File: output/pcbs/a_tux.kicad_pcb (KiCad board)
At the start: 2 copper layers, 136.8 x 108.6 mm, 39 parts

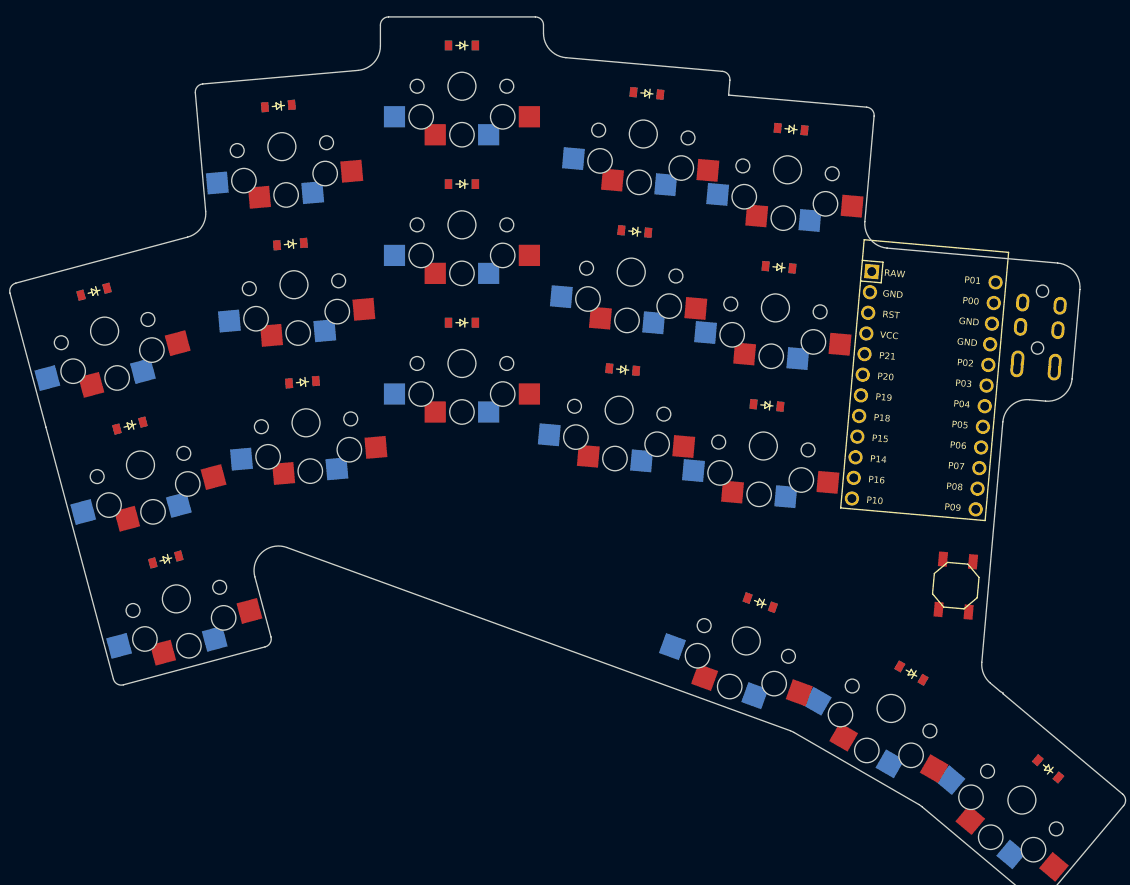
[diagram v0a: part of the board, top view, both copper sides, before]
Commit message: Added hotswap + solder option for switches, moved diode locations, moved stuff around to make routing easier
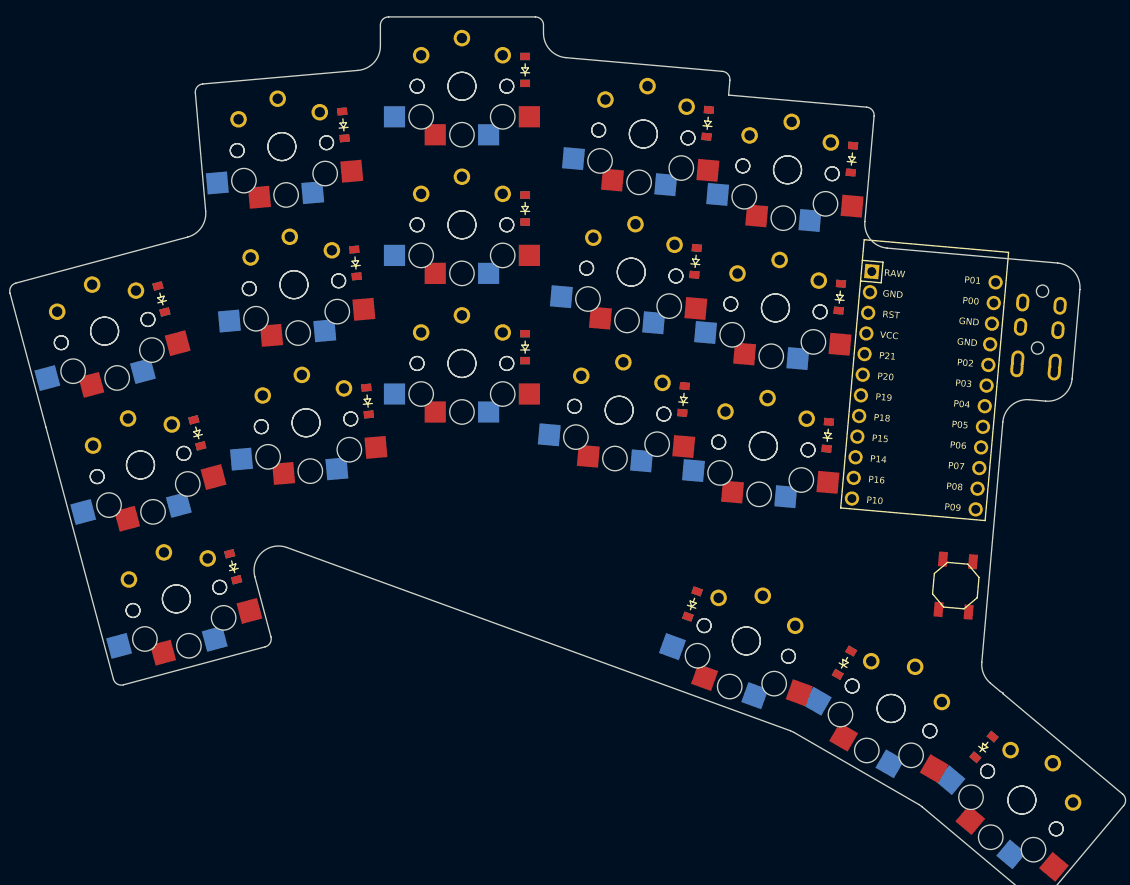
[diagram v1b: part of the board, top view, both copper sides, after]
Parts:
- added S19, S20: , PG1350, F.Cu at (67.9, -22.6)
- added S21, S22: , PG1350, F.Cu at (69.4, -39.5)
- added S23, S24: , PG1350, F.Cu at (70.9, -56.4)
- added S25, S26: , PG1350, F.Cu at (85.6, -18.2)
- added S27, S28: , PG1350, F.Cu at (87.1, -35.1)
- added S29, S30: , PG1350, F.Cu at (88.6, -52.0)
- added S31, S32: , PG1350, F.Cu at (83.5, 5.74)
- added S33, S34: , PG1350, F.Cu at (101.3, 14.0)
- added S35, S36: , PG1350, F.Cu at (117.3, 25.3)
- moved S18 111.3 mm to (48.6, -62.3), turned to 0 degrees
- moved S17 92.7 mm to (48.6, -62.3), turned to 180 degrees
- moved S16 61.8 mm to (48.6, -45.3), turned to 0 degrees
- moved S11 45.5 mm to (26.5, -54.9), turned to 185 degrees
- moved S12 44.4 mm to (26.5, -54.9), turned to 5 degrees
- moved S10 42.7 mm to (28.0, -38.0), turned to 5 degrees
- moved S15 40.5 mm to (48.6, -45.3), turned to 180 degrees
- moved S14 39.0 mm to (48.6, -28.3), turned to 0 degrees
- moved S13 38.3 mm to (48.6, -28.3), turned to 180 degrees
- moved S9 31.9 mm to (28.0, -38.0), turned to 185 degrees
- moved S6 31.4 mm to (4.80, -32.3), turned to 15 degrees
- moved S8 30.9 mm to (29.5, -21.0), turned to 5 degrees
- moved S5 23.9 mm to (4.80, -32.3), turned to 195 degrees
- moved S4 21.0 mm to (9.20, -15.8), turned to 15 degrees
- moved S7 20.5 mm to (29.5, -21.0), turned to 185 degrees
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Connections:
- S10 pad 1: index_bottom -> ring_home
- S10 pad 2: P6 -> P8
- S11 pad 1: index_home -> ring_top
- S11 pad 2: P6 -> P8
- S12 pad 1: index_top -> ring_top
- S12 pad 2: P6 -> P8
- S13 pad 1: inner_bottom -> middle_bottom
- S13 pad 2: P5 -> P7
- S14 pad 1: inner_home -> middle_bottom
- S14 pad 2: P5 -> P7
- S15 pad 1: inner_top -> middle_home
- S15 pad 2: P5 -> P7
- S16 pad 1: first_only -> middle_home
- S17 pad 1: second_only -> middle_top
- S17 pad 2: P6 -> P7
- S18 pad 1: third_only -> middle_top
- S18 pad 2: P5 -> P7
- S2 pad 1: pinky_home -> pinky_bottom
- S3 pad 1: pinky_top -> pinky_home
- S4 pad 1: ring_bottom -> pinky_home
- S4 pad 2: P8 -> P9
- S5 pad 1: ring_home -> pinky_top
- S5 pad 2: P8 -> P9
- S6 pad 1: ring_top -> pinky_top
- S6 pad 2: P8 -> P9
- S7 pad 1: middle_bottom -> ring_bottom
- S7 pad 2: P7 -> P8
- S8 pad 1: middle_home -> ring_bottom
- S8 pad 2: P7 -> P8
- S9 pad 1: middle_top -> ring_home
- S9 pad 2: P7 -> P8

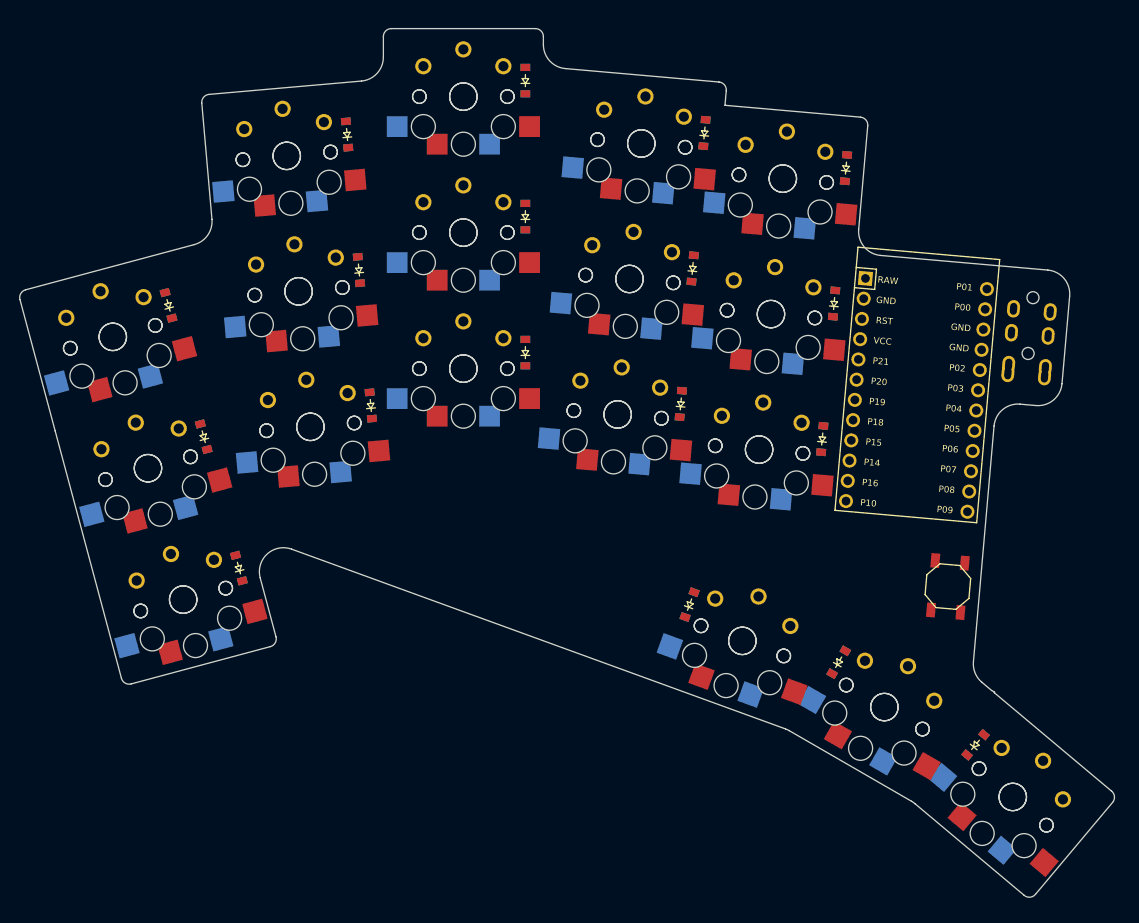
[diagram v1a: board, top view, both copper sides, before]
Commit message: Rotated the outer thumb for 1.5u or 2u keycap.
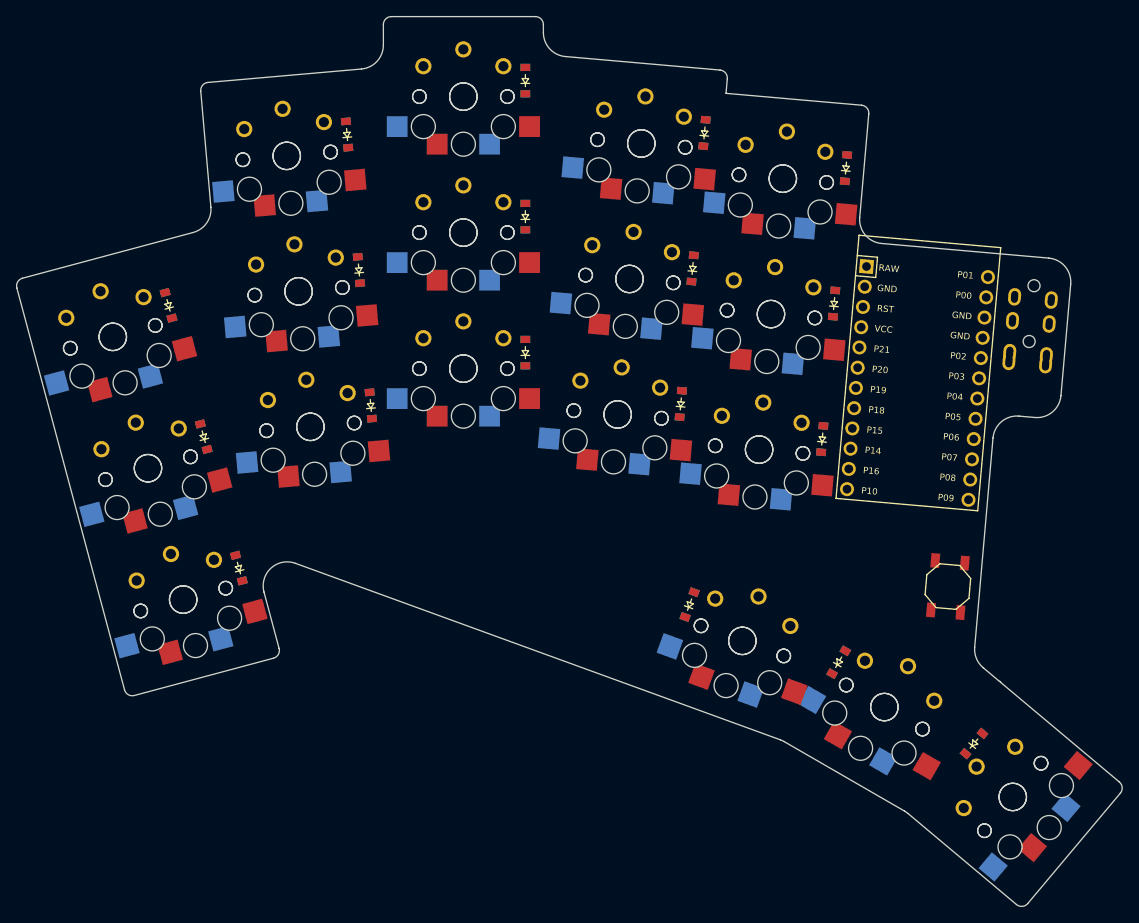
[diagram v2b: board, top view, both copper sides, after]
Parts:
- moved MCU1 1.50 mm to (105.4, -26.5)
- moved REF** 1.50 mm to (122.4, -40.0)
- moved D18 0.25 mm to (112.5, 18.6)
- turned S35 to 230 degrees
- turned S36 to 50 degrees
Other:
- board size 136.8 x 108.6 mm -> 138.2 x 111.2 mm

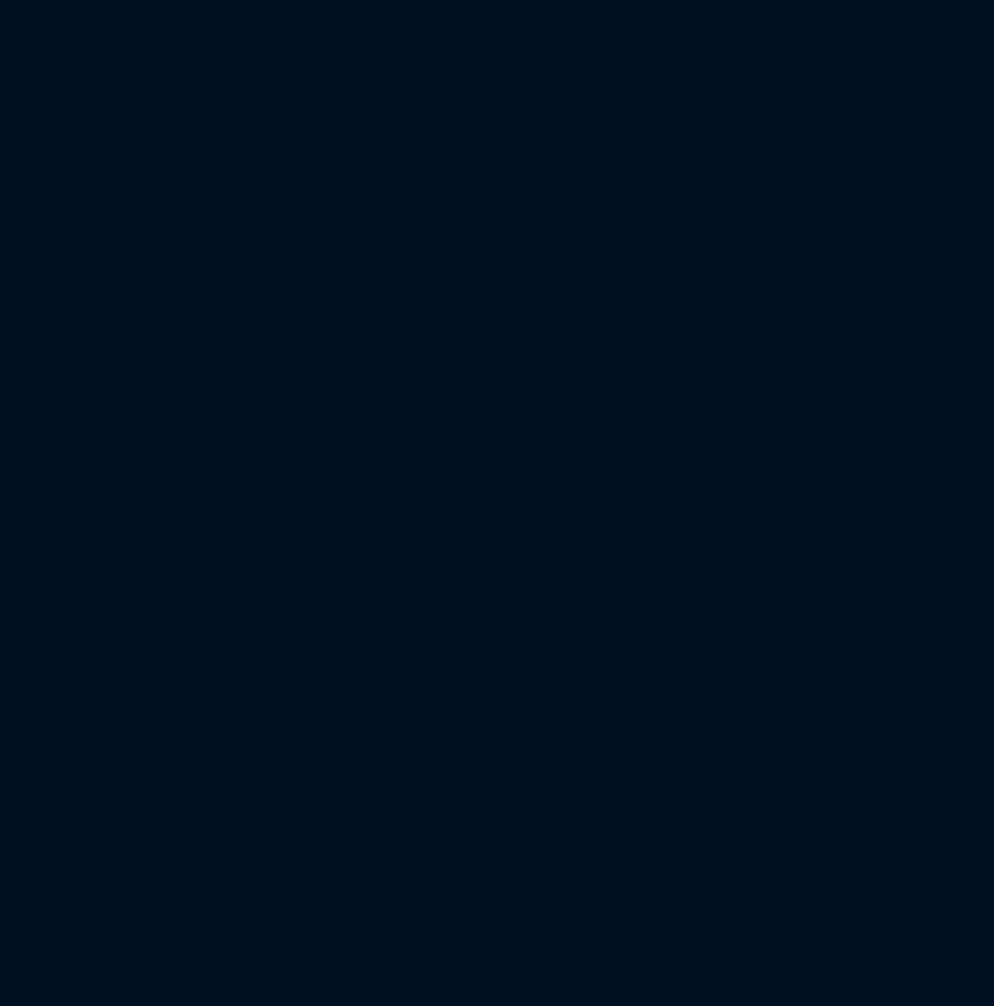
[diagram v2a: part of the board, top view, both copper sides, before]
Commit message: Added Split KB's Puck footprint
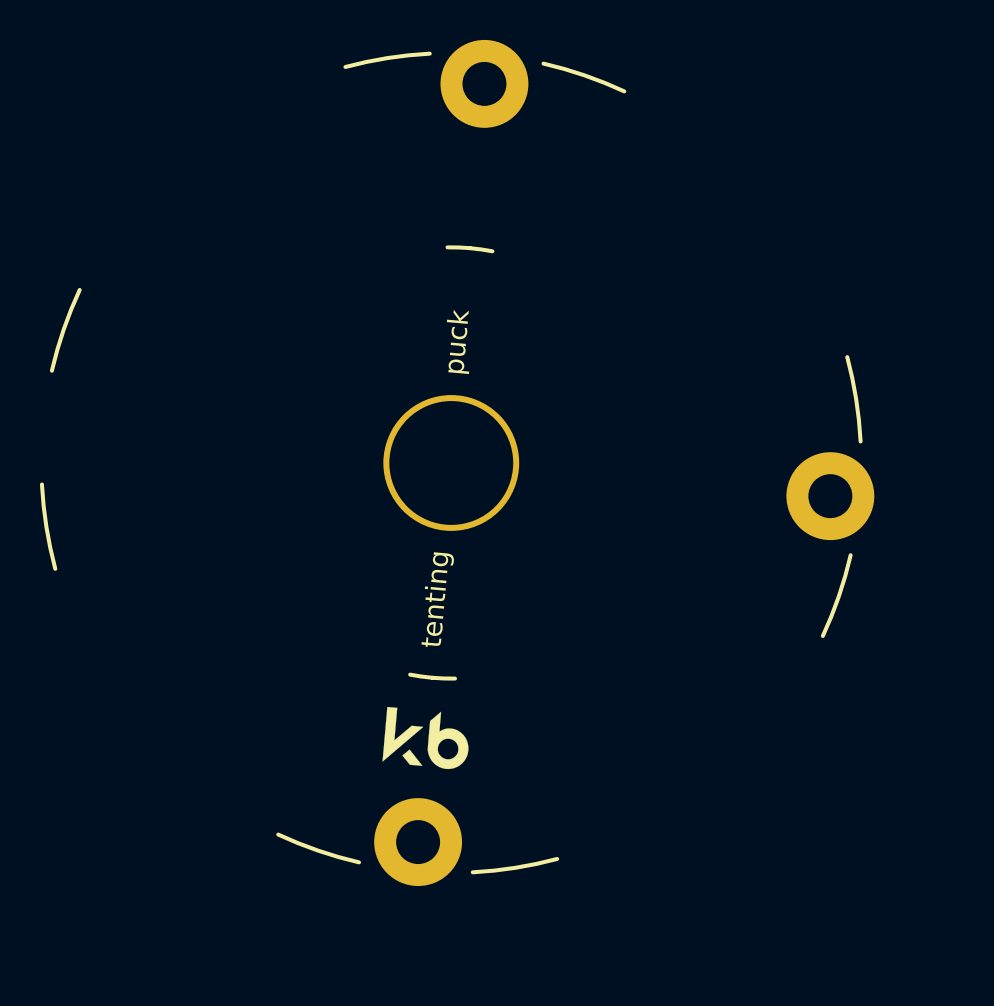
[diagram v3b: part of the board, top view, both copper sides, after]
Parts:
- added _1: Tenting Puck, Tenting Puck, F.Cu at (-112.2, -52.5)

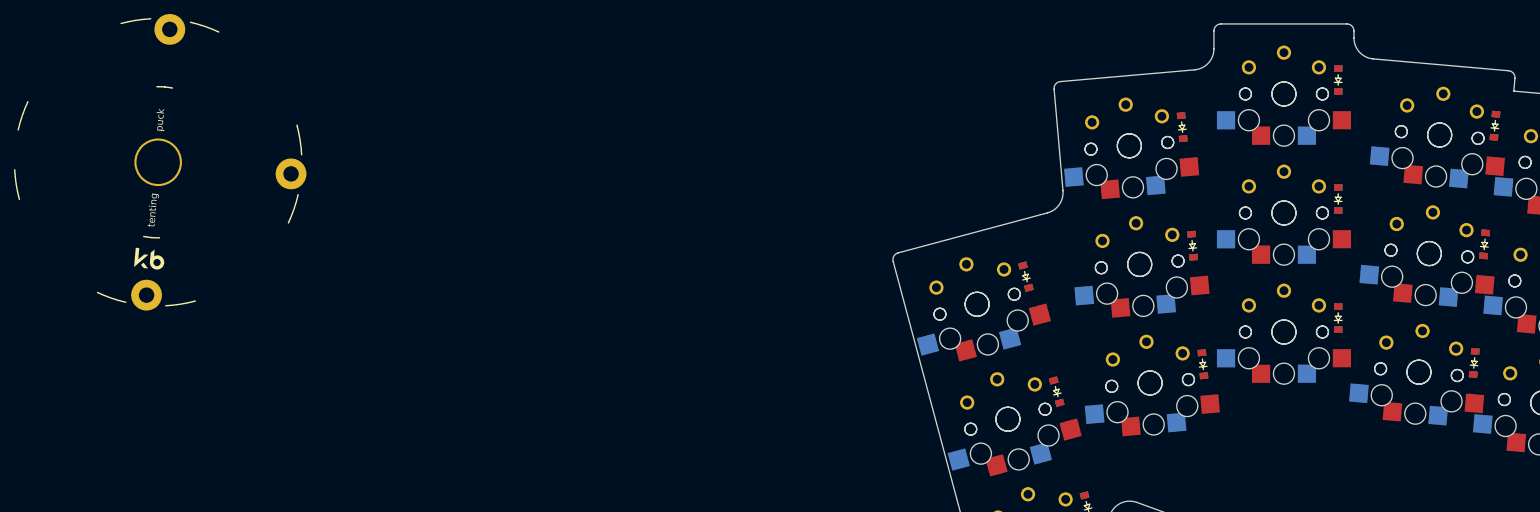
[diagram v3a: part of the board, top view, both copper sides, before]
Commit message: Add puck back to the PCB, fix puck footprint.  Added reversible header footprint
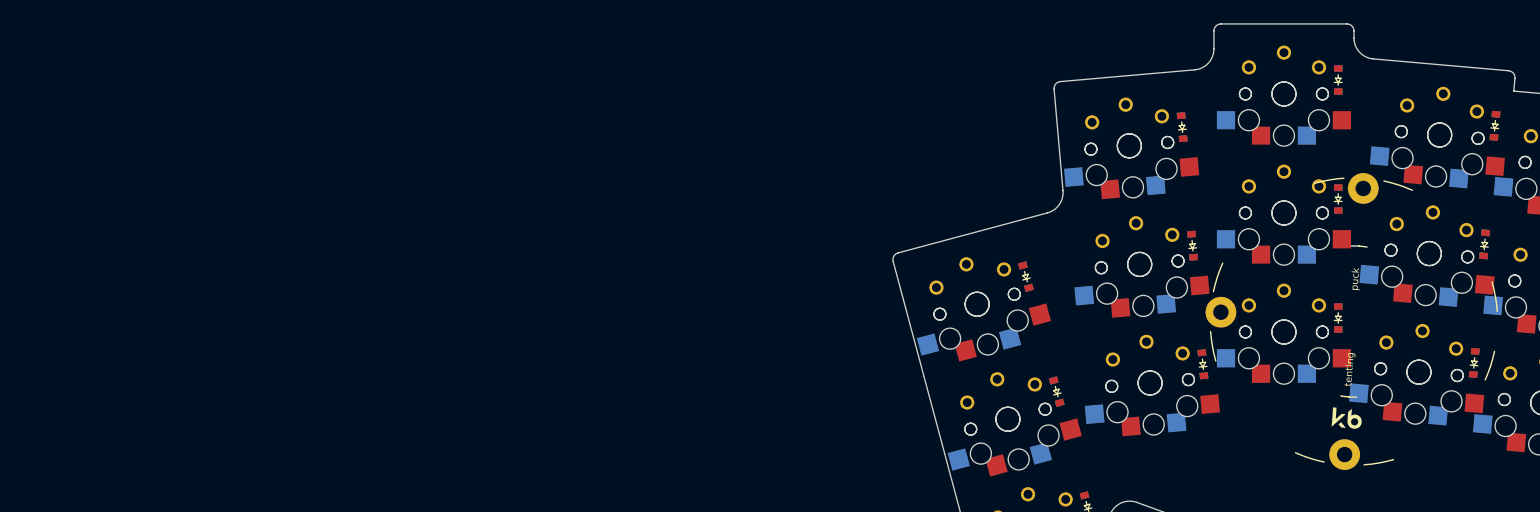
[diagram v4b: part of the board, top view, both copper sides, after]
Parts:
- moved _1 172.3 mm to (58.6, -29.8), turned to -4 degrees
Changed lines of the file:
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@@
       )
 (module "Tenting Puck" (layer F.Cu)
-  (at -112.16671790000001 -52.5371352 -5)
+  (at 58.624363 -29.7933885 -4)
   (fp_text reference "_1" (at 7.6835 1.4605) (layer F.Fab)
     hide
@@
   (fp_arc (start 0 0) (end -20.32 2.8575) (angle -11.96501054) (layer B.SilkS) (width 0.2))
   (fp_arc (start 0 0) (end -20.32 -2.8575) (angle 11.96500434) (layer B.SilkS) (width 0.2))
-  (fp_text user tenting (at -0.1905 6.858 85) (layer F.SilkS)
+  (fp_text user tenting (at -0.1905 6.858 86) (layer F.SilkS)
     (effects (font (size 1 1) (thickness 0.1)))
   )
-  (fp_text user puck (at -0.254 -6.0325 85) (layer F.SilkS)
+  (fp_text user puck (at -0.254 -6.0325 86) (layer F.SilkS)
     (effects (font (size 1 1) (thickness 0.1)))
   )
-  (fp_text user tenting (at -0.254 -6.9215 85) (layer B.SilkS)
+  (fp_text user tenting (at -0.254 -6.9215 86) (layer B.SilkS)
     (effects (font (size 1 1) (thickness 0.1)) (justify mirror))
   )
-  (fp_text user puck (at -0.1905 6.0325 85 unlocked) (layer B.SilkS)
+  (fp_text user puck (at -0.1905 6.0325 86 unlocked) (layer B.SilkS)
     (effects (font (size 1 1) (thickness 0.1)) (justify mirror))
   )
@@
     (xy 1.990108 15.13408) (xy 2.080952 15.226356) (xy 2.080952 12.484486) (xy 1.584498 12.484486)
     (xy 1.584498 14.118044)) (layer B.SilkS) (width 0.01))
-  (pad "" thru_hole circle (at 0 0 -5) (size 6.8 6.8) (drill 6.2) (layers *.Cu *.Mask))
-  (pad 1 thru_hole circle (at 0 -19.05 -5) (size 4.4 4.4) (drill 2.2) (layers *.Cu *.Mask))
-  (pad 1 thru_hole circle (at 19.05  0 -5) (size 4.4 4.4) (drill 2.2) (layers *.Cu *.Mask))
-  (pad 1 thru_hole circle (at 0  19.05 -5) (size 4.4 4.4) (drill 2.2) (layers *.Cu *.Mask))
+  (pad 1 thru_hole circle (at 0 -19.05 -4) (size 4.4 4.4) (drill 2.2) (layers *.Cu *.Mask))
+  (pad 1 thru_hole circle (at 0  19.05 -4) (size 4.4 4.4) (drill 2.2) (layers *.Cu *.Mask))
+  (pad 1 thru_hole circle (at -19.05 0 -4) (size 4.4 4.4) (drill 2.2) (layers *.Cu *.Mask))
 )
     (module E73:SW_TACT_ALPS_SKQGABE010 (layer F.Cu)
